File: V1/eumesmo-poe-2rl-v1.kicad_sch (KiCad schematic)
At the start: 56 parts, among them J1 USB_C_Receptacle_USB2.0, J3 RJ45 JACK, Q1 UMH3N, Q3 WPM2015-3/TR, Q4 LMUN2211LT1G, SW1 RESET, U1 CH340K, U2 ESP32-WROOM-32UE-N16, U3 LAN8710A

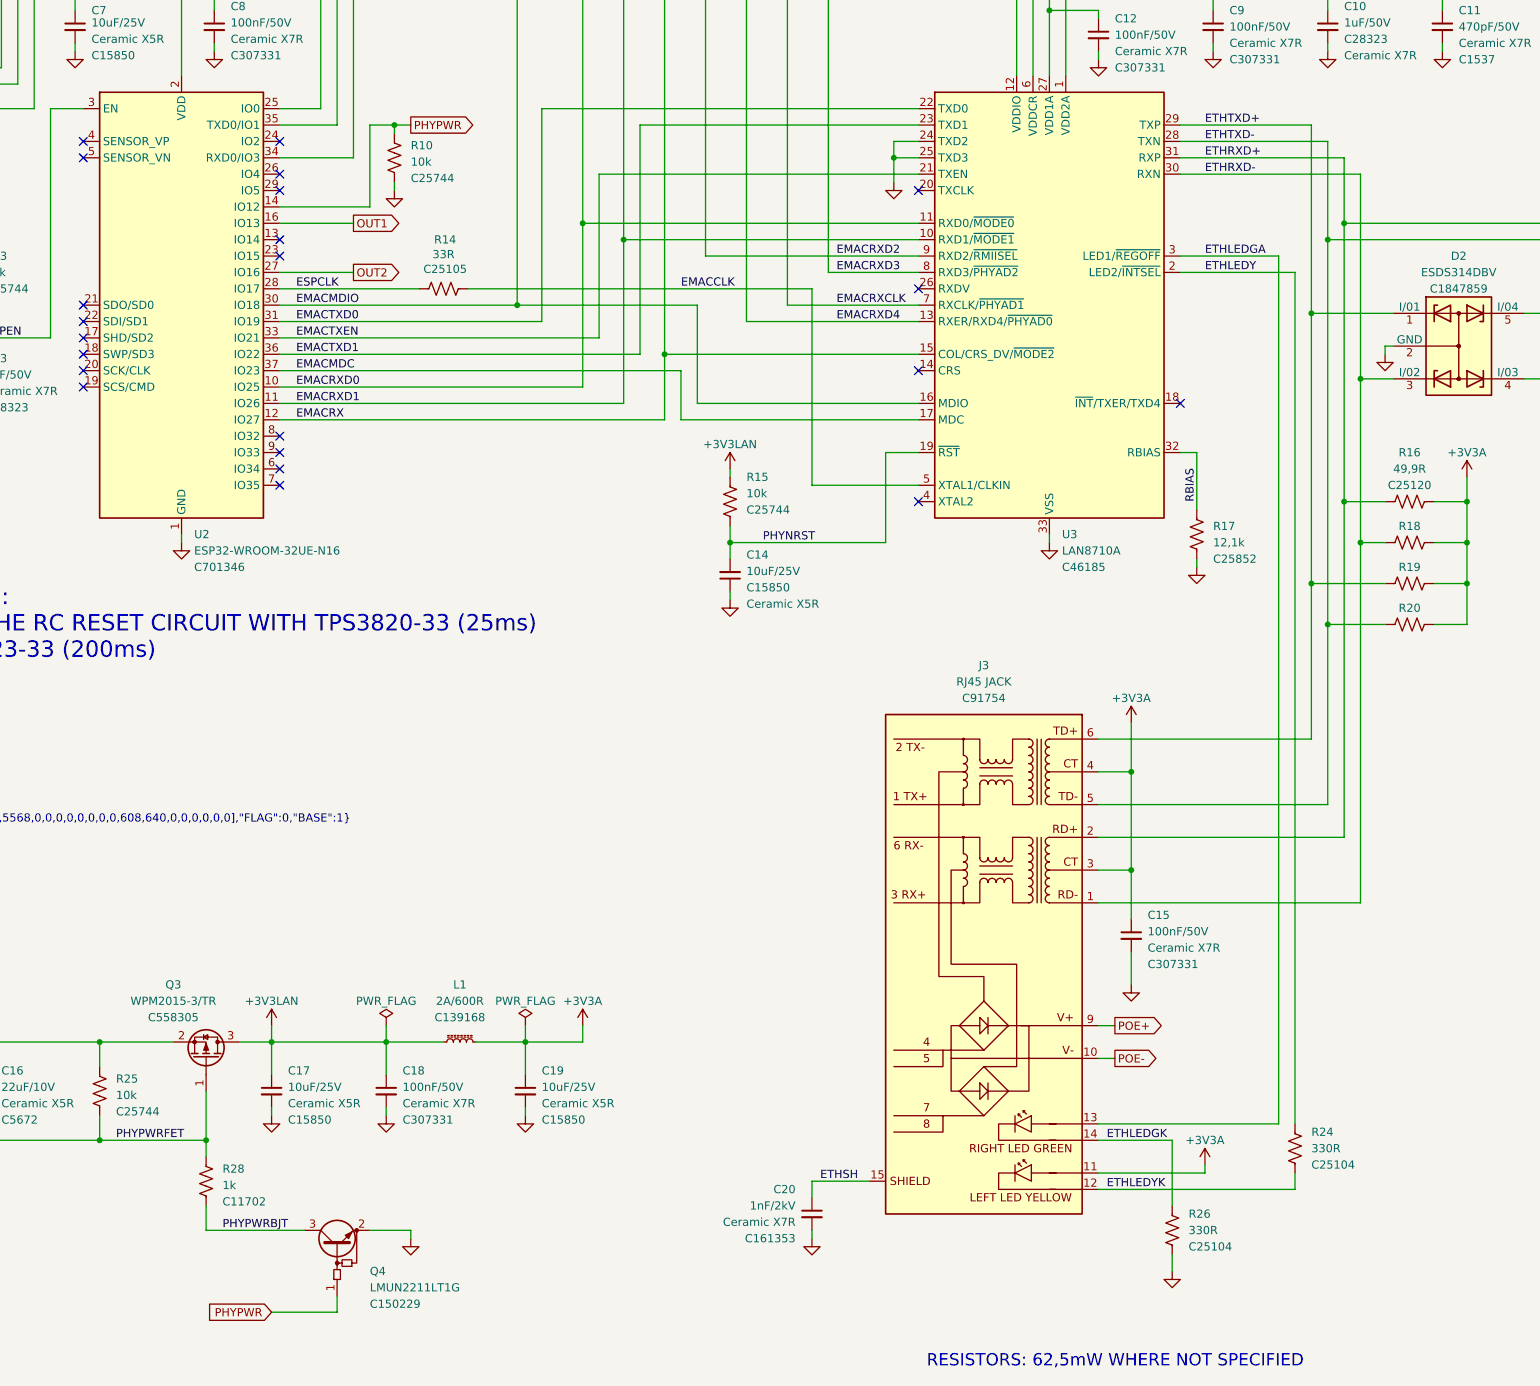
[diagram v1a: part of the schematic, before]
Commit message: Added CPU health LED
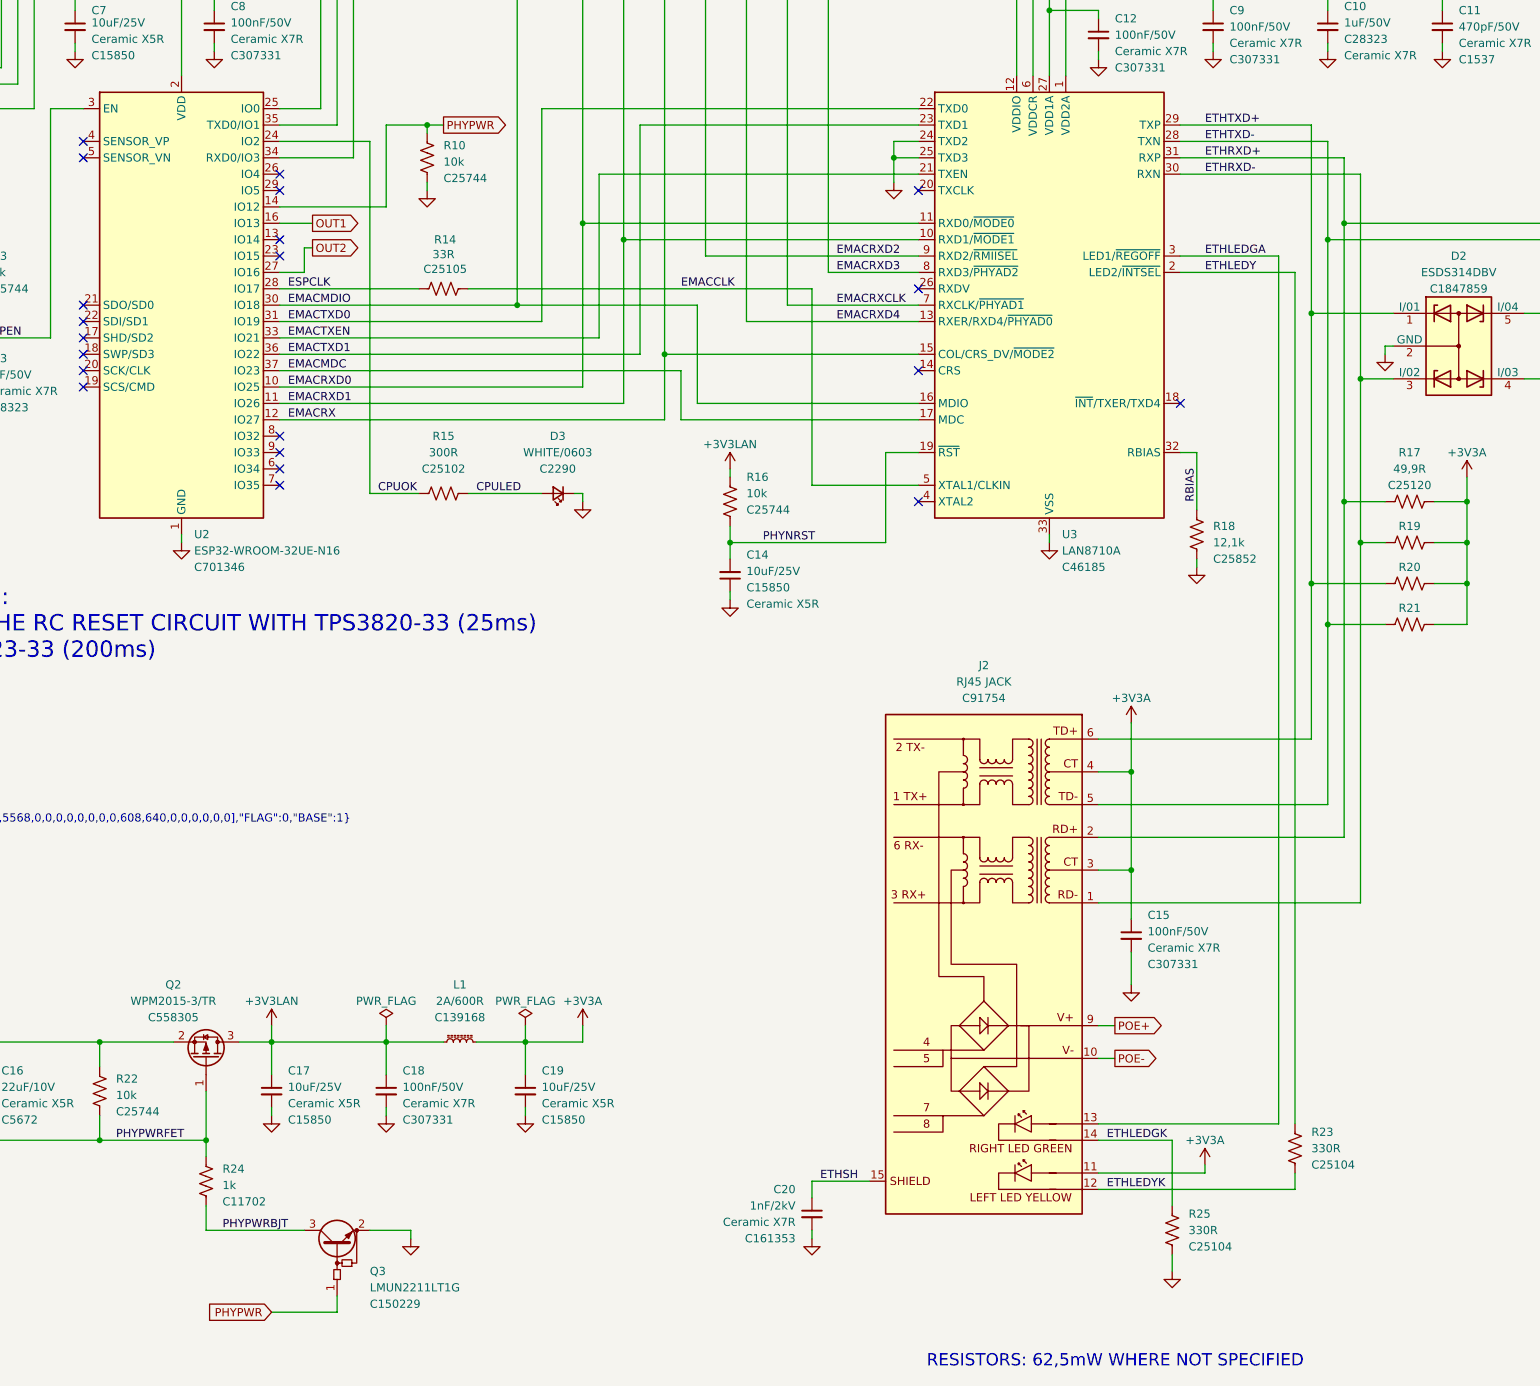
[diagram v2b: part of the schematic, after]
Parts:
- added D3: WHITE/0603, Tales:LED_0603_1608Metric, symbol Device:LED_Small
- added R15: 300R, Tales:R_0402_1005Metric, symbol Device:R_US
- renumbered J3 to J2, Q3 to Q2, Q4 to Q3, R15 to R16, R16 to R17, R17 to R18, R18 to R19, R19 to R20, R20 to R21, R25 to R22, R24 to R23, R28 to R24, R26 to R25
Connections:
- net GND: now also D3.1 (K)
- net CPUOK: now reaches U2.24 (IO2)
- net CPUOK: now also R15.1
- new net CPULED: D3.2 (A), R15.2
- no-connect marks 25 -> 24
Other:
- moved on the sheet: R10
